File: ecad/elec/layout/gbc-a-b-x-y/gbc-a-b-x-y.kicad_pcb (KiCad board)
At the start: 2 copper layers, 10 parts

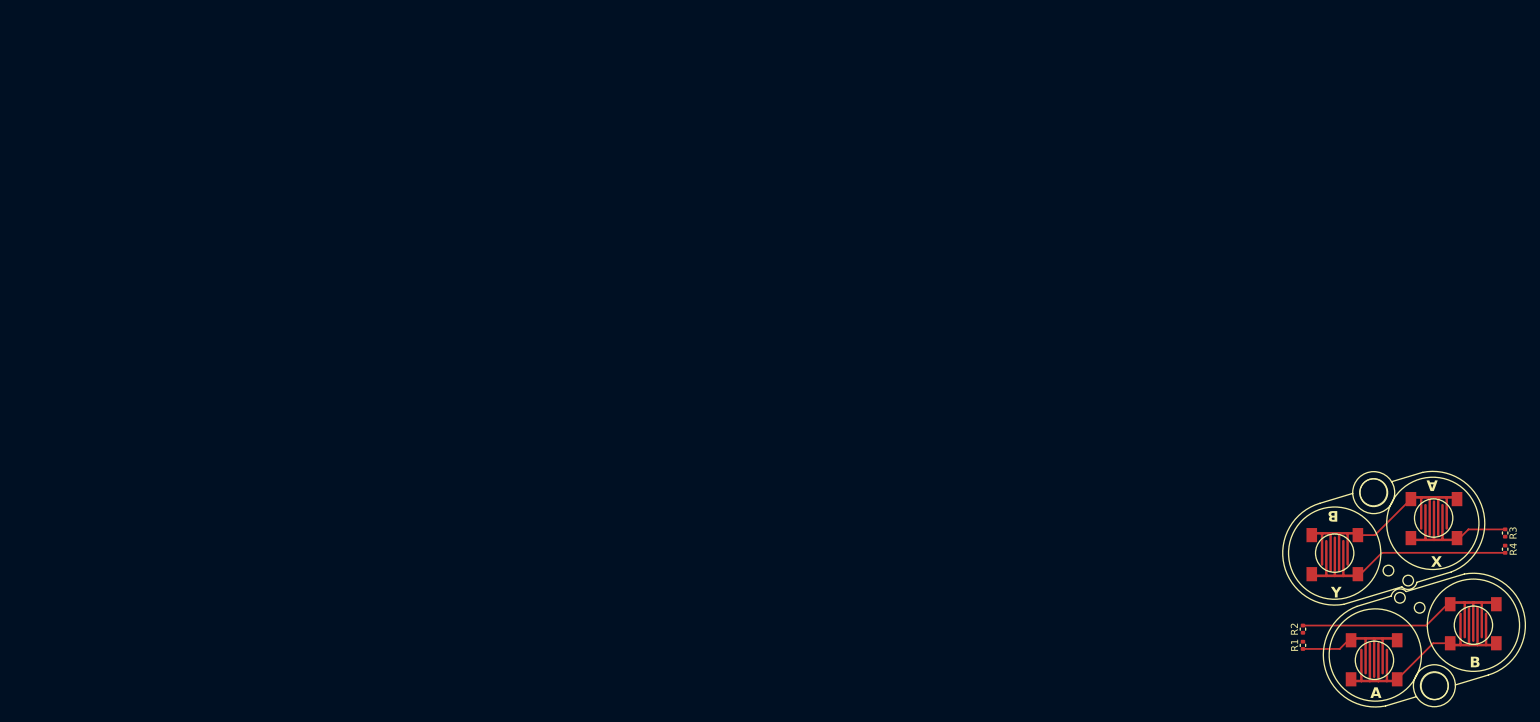
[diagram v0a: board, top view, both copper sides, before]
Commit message: feat(ecad): Update ECAD to support latest atopile and fix some bugs (#119)
* feat(ecad): Update ecad / atopile and improve workflow

* add step file to repo

* add box-3 step file

* improve workflow

* update the action to latest and fix some bugs / spurious issues

* remove legacy files

* update readme

* update deprecations

* improve placement of components and robustness of scripts

* nudge layouts some

* further layout changes

* fixing some issues

* fix broken ci

* minor update

* simple layout

* update to work with latest atopile services (lack thereof)

* update routing

* fix(ecad): vendor atopile registry package for CI builds

packages.atopileapi.com no longer resolves (taken down in the 0.16
platform migration, like the components API), so dependency resolution
of atopile/ti-tps63020@0.4.0 fails in CI and on any machine without a
warm .ato/modules. Commit the installed package (sans .cache) so
`ato build` finds it via its installed-package path and never contacts
the dead registry.

Co-Authored-By: Claude Fable 5 <noreply@anthropic.com>

* fix(ecad): keep vendored package byte-exact (no EOL normalization)

ato validates installed packages against the file hashes in
.package_meta.json; git's CRLF->LF normalization of the STEP files
changed their bytes on checkout, making CI fail with "Package has
local modifications". Exempt ecad/.ato/modules from text normalization
and re-commit the original bytes.

Co-Authored-By: Claude Fable 5 <noreply@anthropic.com>

* fix(ci): disable baked-in ATO_FROZEN and normalize base layout serialization

The atopile-kicad docker image sets ATO_FROZEN=1, silently forcing CI
builds into frozen mode, which fails on phantom in-memory diffs
(locked-attribute defaults, arc direction normalization) that never
reach the file on disk. Pass ATO_FROZEN=0 from the workflow — we verify
layout stability ourselves via canonicalize + git diff.

Also re-serialize box-emu-base.kicad_pcb through the same container
build + canonicalize pip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
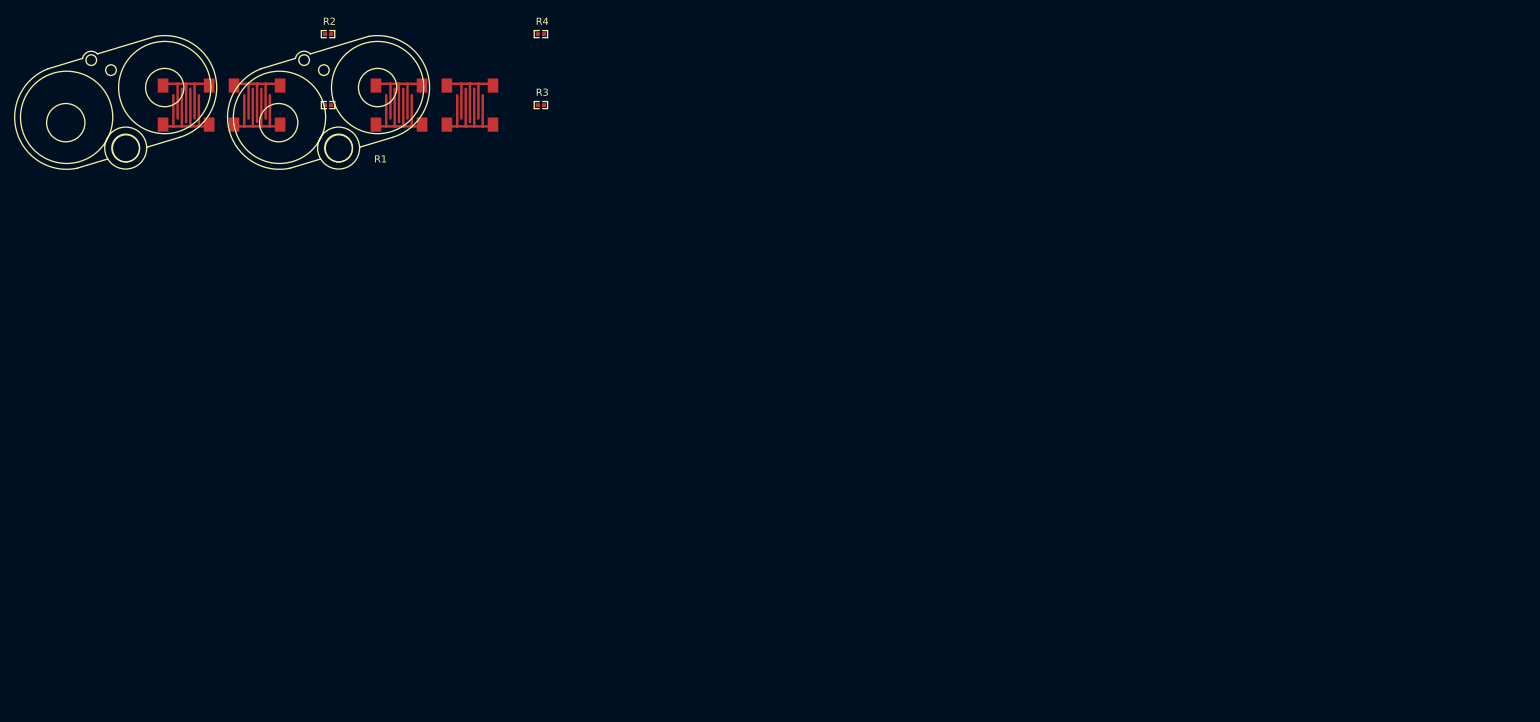
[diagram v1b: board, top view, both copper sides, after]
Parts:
- removed U1, U4: , lib:GAMEBOY_COLOR_A_B_BUTTON_MEMBRANE
- removed U2, U3, U5, U6: , lib:GBC_A_B_BUTTON
- added MECH1: , GBC_A_B_MEMBRANE:GAMEBOY_COLOR_A_B_BUTTON_MEMBRANE, F.Cu at (0.00, 0.00)
- added MECH2: , GBC_A_B_MEMBRANE:GAMEBOY_COLOR_A_B_BUTTON_MEMBRANE, F.Cu at (30.0, 0.00)
- added SW1: , GBC_A_B_BUTTON:GBC_A_B_BUTTON, F.Cu at (10.0, 0.00)
- added SW2: , GBC_A_B_BUTTON:GBC_A_B_BUTTON, F.Cu at (20.0, 0.00)
- added SW3: , GBC_A_B_BUTTON:GBC_A_B_BUTTON, F.Cu at (40.0, 0.00)
- added SW4: , GBC_A_B_BUTTON:GBC_A_B_BUTTON, F.Cu at (50.0, 0.00)
- R1, R2, R3, R4: value 62.5mW Thick Film Resistors 50V ±100ppm/℃ ±1% 10kΩ 0402 Chip Resistor - Surface Mount ROHS -> 10kΩ ±5%; footprint lib:R0402 -> UNI_ROYAL_0402WGF1002TCE:R0402
- moved R2 161.0 mm to (30.0, -10.0), turned to 0 degrees
- moved R1 157.1 mm to (30.0, 0.00), turned to 0 degrees
- moved R4 154.1 mm to (60.0, -10.0), turned to 0 degrees
- moved R3 148.7 mm to (60.0, 0.00), turned to 0 degrees
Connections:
- net vcc renamed hv
- R1 pad 2: a -> line
- R2 pad 2: b -> b_btn-out-line
- R3 pad 2: x -> a-line
- R4 pad 2: y -> b-line
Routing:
- net gnd: track 46.0 -> 0.00 mm
- net y: track 28.3 -> 0.00 mm
- net b: track 28.3 -> 0.00 mm
- net x: track 13.7 -> 0.00 mm
- net a: track 13.7 -> 0.00 mm
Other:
- board text removed: "A"
- board text removed: "B"
- board text removed: "X"
- board text removed: "Y"
